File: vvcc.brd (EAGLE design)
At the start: 49 x 50 mm, 51 parts, among them IC1 MCP40D19T-5K, IC2 RP2040, IC3 NCP1117LPST33T3G, IC4 16MB_Flash, IC5 LD117ADT-TR, IC6 CLXC8T245QRHLRQ1, J1 Micro-B, J2 302-S301, J3 302-S301, Q1 12MHz

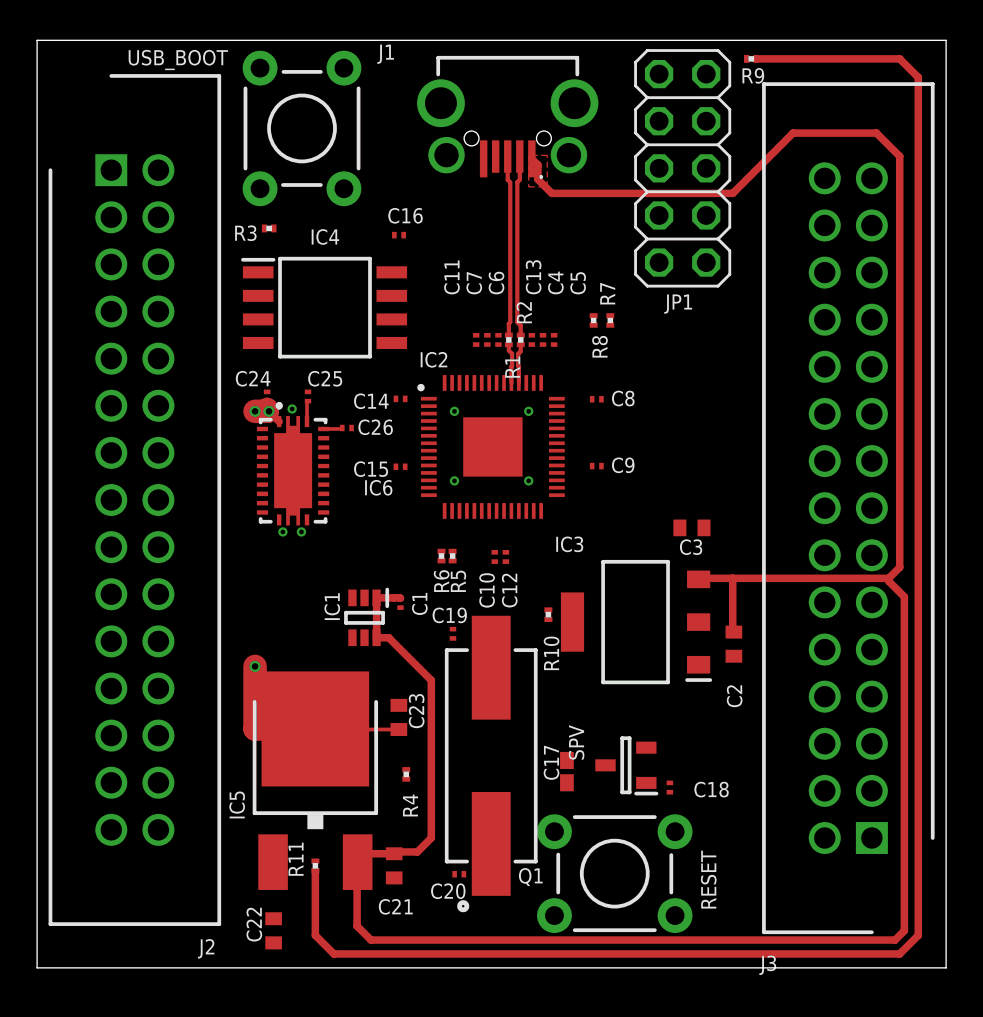
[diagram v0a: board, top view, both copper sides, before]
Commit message: Change the layout a little to group +5v closer together
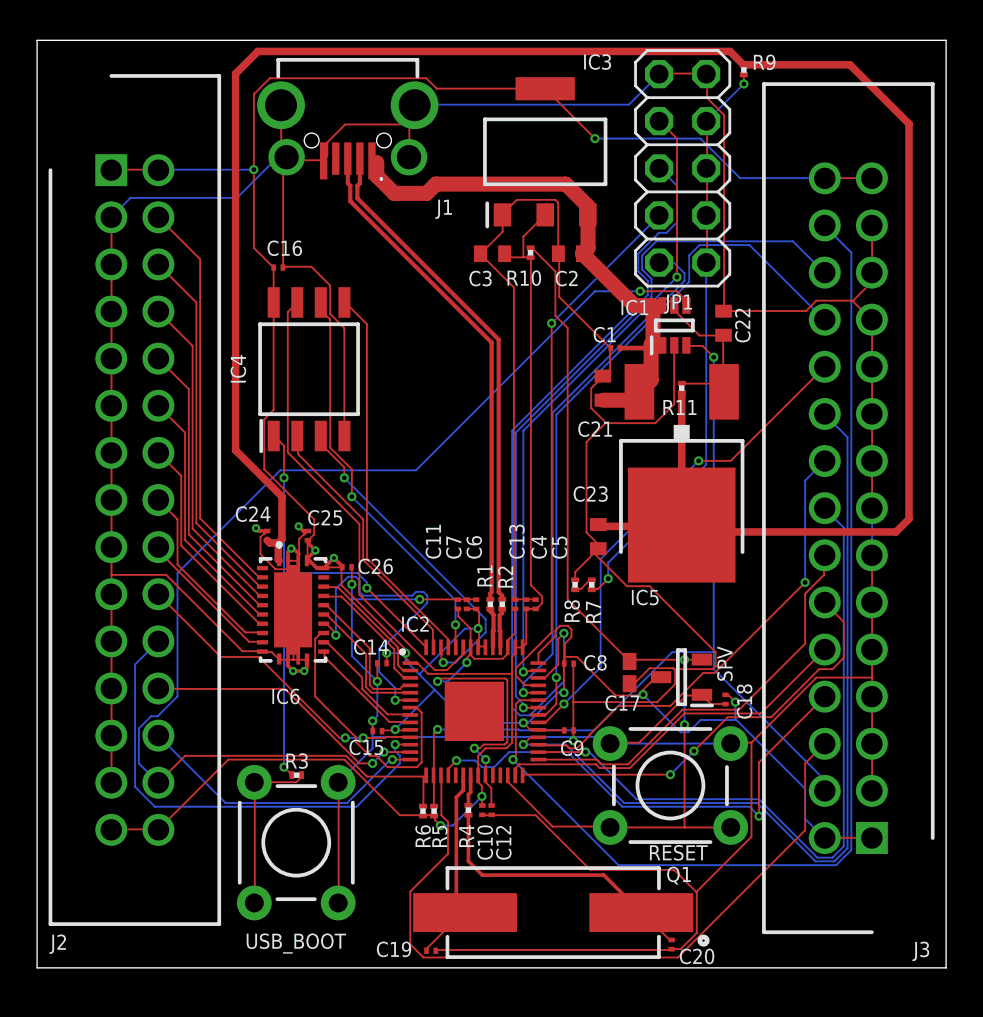
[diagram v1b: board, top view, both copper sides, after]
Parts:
- moved C22 40.8 mm to (37.0, 34.8), turned to 90 degrees
- moved USB_BOOT 38.5 mm to (14.0, 6.75), turned to 270 degrees
- moved R11 32.5 mm to (34.8, 31.2)
- moved R3 29.5 mm to (14.0, 10.4), turned to 180 degrees
- moved C21 28.1 mm to (30.5, 31.2), turned to 90 degrees
- moved IC3 25.8 mm to (27.4, 44.0), turned to 90 degrees
- moved IC5 25.3 mm to (34.8, 26.2), turned to 180 degrees
- moved IC1 23.0 mm to (34.4, 34.6), turned to 90 degrees
- moved C2 22.8 mm to (28.8, 38.5), turned to 180 degrees
- moved R10 19.5 mm to (26.6, 38.5)
- moved C3 18.3 mm to (24.6, 38.5)
- moved C1 18.0 mm to (31.2, 33.4), turned to 180 degrees
- moved C19 17.1 mm to (21.2, 0.92), turned to 0 degrees
- moved C23 14.5 mm to (30.2, 23.2), turned to 270 degrees
- moved C8 14.3 mm to (28.7, 16.4)
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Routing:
- net GND: track 0.00 -> 357.2 mm, vias 7 -> 10
- net +3V3: track 2.20 -> 208.0 mm, vias 0 -> 14
- net +5V: track 133.1 -> 31.6 mm
- net GPIO12: track 0.00 -> 64.2 mm, vias 0 -> 1
- net GPIO25: track 0.00 -> 59.5 mm, vias 0 -> 1
- net !RESET!: track 0.00 -> 51.1 mm, vias 0 -> 2
- net GPIO13: track 0.00 -> 48.5 mm, vias 0 -> 2
- net GPIO21: track 0.00 -> 45.3 mm, vias 0 -> 1
- net ADC2: track 0.00 -> 43.3 mm, vias 0 -> 1
- net GPIO14: track 0.00 -> 39.6 mm
- net GPIO24: track 0.00 -> 39.5 mm, vias 0 -> 1
- net GPIO19: track 0.00 -> 37.7 mm, vias 0 -> 1
- net GPIO23: track 0.00 -> 37.6 mm, vias 0 -> 1
- net ADC3: track 0.00 -> 34.4 mm, vias 0 -> 2
- net N$9: track 0.00 -> 31.5 mm, vias 0 -> 2
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- removed copper zone on layer 1, net +5V

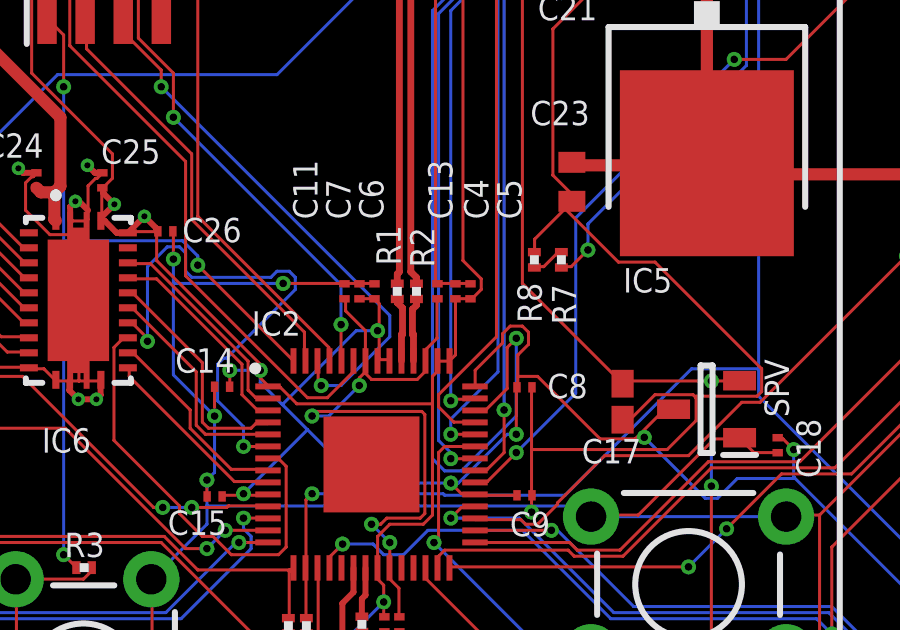
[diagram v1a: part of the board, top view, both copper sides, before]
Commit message: Add in a missing 0.1uF capacitor on +3v3
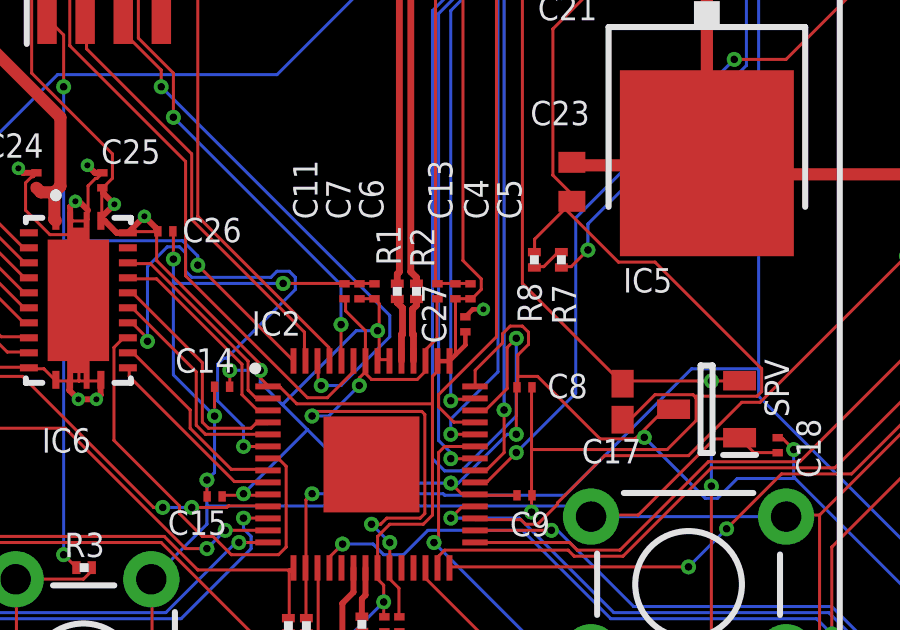
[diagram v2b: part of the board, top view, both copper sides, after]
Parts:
- added C27: 1uF, rcl:C0201
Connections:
- net +3V3: now also C27.1
- net GND: now also C27.2
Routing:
- net +3V3: track 208.0 -> 209.2 mm
- net GND: track 357.2 -> 358.0 mm, vias 10 -> 11
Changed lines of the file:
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@@
 <attribute name="VALUE" x="16.065" y="19.695" locked="yes" size="1.27" layer="27"/>
+</element>
+<element name="C27" library="rcl" library_urn="urn:adsk.eagle:library:334" package="C0201" package3d_urn="urn:adsk.eagle:package:23690/2" value="1uF" x="26.7" y="18.5" smashed="yes" rot="R90">
+<attribute name="NAME" x="26.065" y="17.865" size="0.8128" layer="25" rot="R90"/>
+<attribute name="POPULARITY" value="0" x="26.7" y="18.5" size="1.778" layer="27" rot="R90" display="off"/>
+<attribute name="SPICEPREFIX" value="C" x="26.7" y="18.5" size="1.778" layer="27" rot="R90" display="off"/>
+<attribute name="USE" value="0201B102K250CT" x="26.7" y="18.5" size="1.778" layer="27" rot="R90" display="off"/>
+<attribute name="VALUE" x="28.605" y="17.865" size="1.27" layer="27" rot="R90"/>
 </element>
 </elements>
@@
 <wire x1="14.540525" y1="16.640525" x2="14.55" y2="16.65" width="0.2" layer="1"/>
 <wire x1="14.540525" y1="16.140525" x2="14.540525" y2="16.640525" width="0.2" layer="1"/>
+<contactref element="C27" pad="2"/>
+<via x="27.3" y="19" extent="1-16" drill="0.2"/>
+<wire x1="26.7" y1="18.75" x2="26.95" y2="19" width="0.1524" layer="1"/>
+<wire x1="26.95" y1="19" x2="27.3" y2="19" width="0.1524" layer="1"/>
 </signal>
 <signal name="+3V3">
@@
 <wire x1="26.4144" y1="19.3548" x2="26.37" y2="19.35" width="0.1016" layer="1"/>
 <wire x1="26.8224" y1="19.3548" x2="26.87" y2="19.35" width="0.1016" layer="1"/>
-<wire x1="26.37" y1="17.48" x2="26.37" y2="19.35" width="0.1016" layer="1"/>
+<wire x1="26.37" y1="19.35" x2="26.37" y2="17.48" width="0.1016" layer="1"/>
 <wire x1="26.17" y1="17.28" x2="26.37" y2="17.48" width="0.1016" layer="1"/>
-<wire x1="26.162" y1="17.272" x2="25.8064" y2="17.272" width="0.1016" layer="1"/>
 <wire x1="25.8064" y1="17.272" x2="25.77" y2="17.28" width="0.1016" layer="1"/>
 <wire x1="26.162" y1="17.272" x2="26.17" y2="17.28" width="0.1016" layer="1"/>
@@
 <wire x1="15.45" y1="21.55" x2="15.0768" y2="21.55" width="0.2" layer="1"/>
 <wire x1="15.0768" y1="21.55" x2="15.0134" y2="21.6134" width="0.2" layer="1"/>
+<contactref element="C27" pad="1"/>
+<wire x1="26.7" y1="18.25" x2="26.7" y2="17.81" width="0.1524" layer="1"/>
+<wire x1="26.7" y1="17.81" x2="26.37" y2="17.48" width="0.1524" layer="1"/>
+<wire x1="26.37" y1="17.48" x2="26.162" y2="17.272" width="0.1524" layer="1"/>
+<wire x1="26.162" y1="17.272" x2="25.8064" y2="17.272" width="0.1524" layer="1"/>
 </signal>
 <signal name="+1.8_FT">

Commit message: Fix a few errors in the schematic. It is good to connect GND to the chip...
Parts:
- moved C16 9.66 mm to (21.5, 33.1)
- moved IC4 4.07 mm to (17.8, 29.6), turned to 0 degrees
- moved C17 0.75 mm to (31.9, 16.7)
- moved SPV 0.75 mm to (34.7, 16.4)
- moved C18 0.75 mm to (37.1, 15.2)
- moved RESET 0.56 mm to (33.9, 10.3)
- moved USB_BOOT 0.50 mm to (14.0, 6.25)
- moved R3 0.44 mm to (14.2, 10.8)
- moved C25 0.32 mm to (14.3, 23.2), turned to 180 degrees
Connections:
- new net SWCLK: IC2.24, J3.5
- new net SWDIO: IC2.25, J3.7
- net !RESET!: now also J3.3
- net GND: now also IC2.19, IC2.57; no longer J3.3, J3.5, J3.7
- net GPIO8: now also IC6.2
- net GPIO9: now also IC6.22
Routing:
- net GND: track 358.0 -> 112.0 mm, vias 11 -> 21
- net +3V3: track 209.2 -> 47.5 mm, vias 14 -> 16
- net SWDIO: track 0.00 -> 25.8 mm
- net SWCLK: track 0.00 -> 22.4 mm, vias 0 -> 1
- net GPIO8: track 16.8 -> 35.0 mm
- net GPIO21: track 45.3 -> 29.2 mm
- net GPIO25: track 59.5 -> 75.4 mm
- net GPIO14: track 39.6 -> 24.9 mm, vias 0 -> 2
- net !RESET!: track 51.1 -> 63.8 mm, vias 2 -> 0
- net GPIO15: track 27.1 -> 39.8 mm, vias 2 -> 1
- net GPIO22: track 26.8 -> 37.9 mm, vias 2 -> 1
- net LVL4: track 17.5 -> 6.81 mm, vias 2 -> 0
- net QSPI_SD3: track 25.6 -> 15.0 mm
- net QSPI_SD0: track 20.9 -> 10.8 mm
- net QSPI_CLK: track 21.6 -> 13.2 mm, vias 2 -> 0
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
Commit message: Submit for creation
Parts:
- C17: device rcl:C0402K -> rcl:C0402
- JP1: value (none) -> ADC_IO
- RESET: value RESET -> B3F-1005
- USB_BOOT: value USB_BOOT -> B3F-1005
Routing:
- net +3V3: track 47.5 -> 63.7 mm, vias 16 -> 26

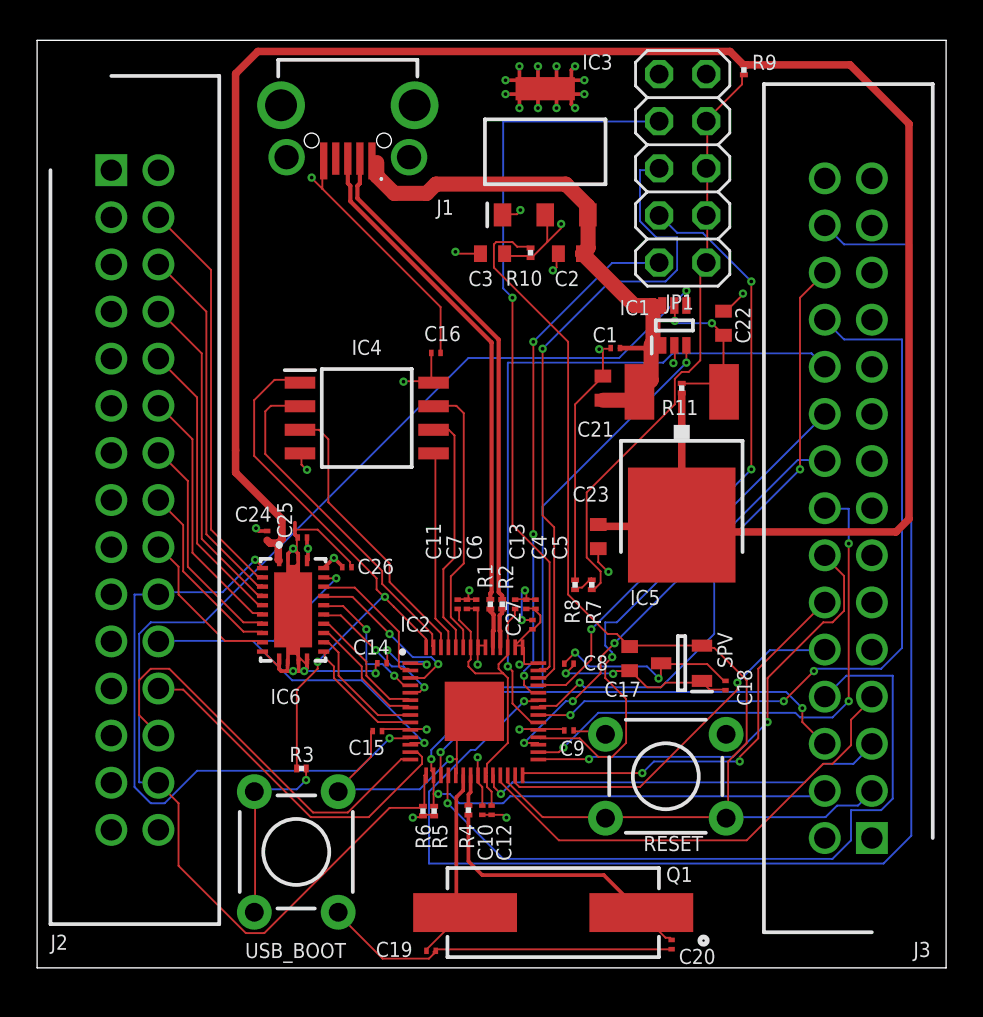
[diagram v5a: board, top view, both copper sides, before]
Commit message: Better board layout - and added LEDs. This was the real submit to nextpcb
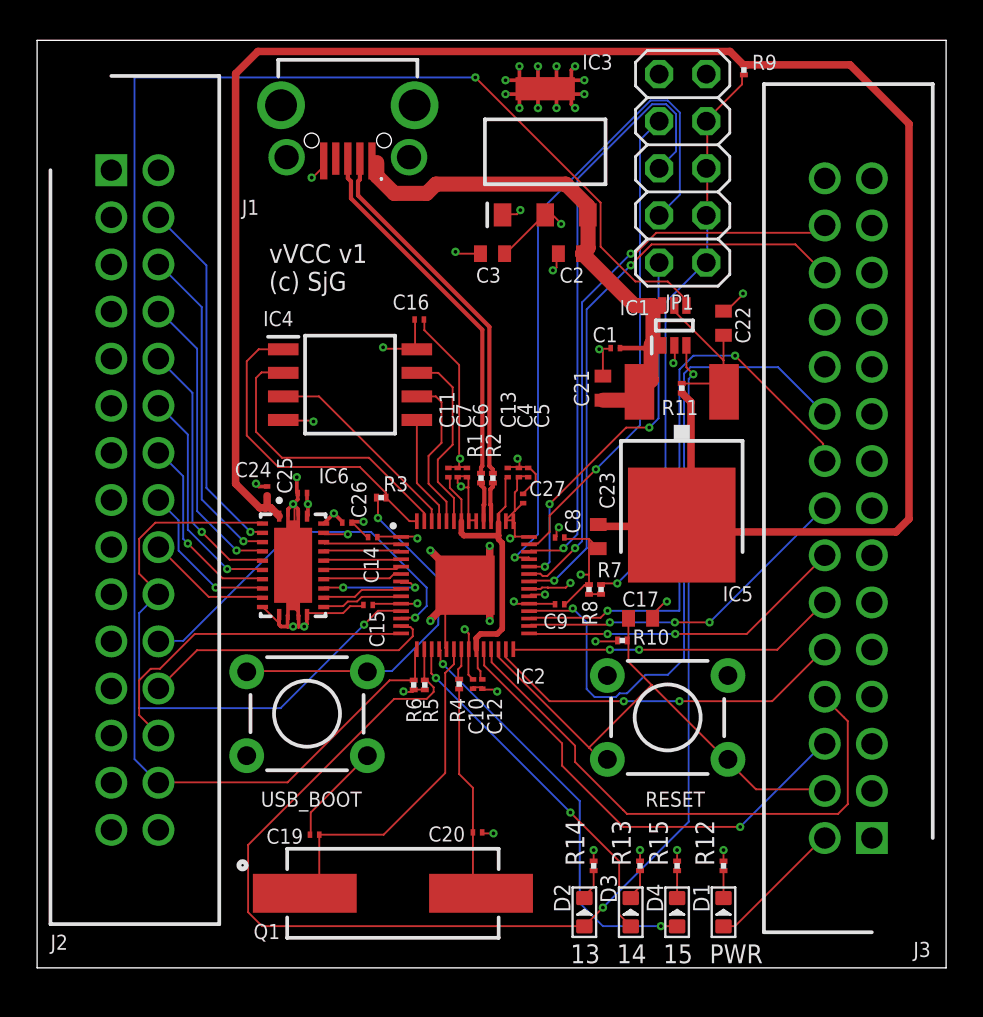
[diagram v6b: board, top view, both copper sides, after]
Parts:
- removed C18: 100nF, rcl:C0201
- removed SPV: MIC803-30D3VM3-TR, x-pi:SOT95P237X111-3N
- added D1, D2, D3, D4: GREEN, Seeed-LED:LED-0603
- added R12, R13, R14, R15: 1K, rcl:R0201
- moved R10 21.5 mm to (31.6, 17.6), turned to 180 degrees
- moved R3 15.2 mm to (18.6, 25.4), turned to 0 degrees
- moved C20 12.1 mm to (23.7, 7.30), turned to 180 degrees
- moved C19 8.87 mm to (15.0, 7.18), turned to 180 degrees
- moved Q1 8.70 mm to (19.2, 4.02), turned to 0 degrees
- moved USB_BOOT 7.47 mm to (14.6, 13.7), turned to 180 degrees
- moved C11 7.12 mm to (22.2, 26.7)
- moved C6 7.12 mm to (23.2, 26.7)
- moved C7 7.12 mm to (22.7, 26.7)
- moved C4 7.11 mm to (26.0, 26.7)
- moved C5 7.11 mm to (26.5, 26.7)
- moved C13 7.11 mm to (25.4, 26.7)
- moved C10 6.82 mm to (23.5, 15.3)
- moved C12 6.82 mm to (24.0, 15.3)
- moved C14 6.82 mm to (18.1, 23.2)
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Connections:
- new net N$1: C19.1, IC2.20, Q1.1
- new net N$2: C20.2, Q1.2, R4.1
- new net N$3: D1.-, R12.1
- new net N$4: D2.-, R14.1
- net !RESET!: now also J3.4; no longer J3.3, SPV.2
- net +3V3: now also D1.+; no longer C18.1, SPV.3
- net GND: now also J3.3, J3.5, J3.7, R12.2, R13.2, R14.2, R15.2; no longer C18.2, SPV.1
- net GPIO13: now also D2.+; no longer J3.4
- net GPIO14: now also D3.+; no longer J3.6
- net GPIO15: now also D4.+; no longer J3.8
- net N$6: now also D3.-, R13.1; no longer C19.1, IC2.20, Q1.2
- net N$8: now also D4.-, R15.1; no longer C20.2, Q1.1, R4.1
- net SWCLK: now also J3.6; no longer J3.5
- net SWDIO: now also J3.8; no longer J3.7
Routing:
- net GPIO25: track 75.4 -> 31.4 mm, vias 1 -> 2
- net GND: track 112.0 -> 76.0 mm, vias 21 -> 28
- net !RESET!: track 63.7 -> 29.3 mm
- net GPIO12: track 71.3 -> 92.8 mm
- net GPIO23: track 42.3 -> 22.2 mm, vias 3 -> 1
- net N$1: track 0.00 -> 18.5 mm
- net GPIO13: track 53.7 -> 71.9 mm, vias 3 -> 2
- net GPIO15: track 39.8 -> 22.6 mm, vias 1 -> 2
- net GPIO22: track 37.9 -> 21.9 mm
- net !QSPI_SS!: track 31.5 -> 17.5 mm, vias 2 -> 0
- net N$8: track 15.2 -> 1.48 mm
- net ADC3: track 39.5 -> 26.0 mm
- net N$2: track 0.00 -> 11.5 mm
- net GPIO19: track 29.8 -> 18.6 mm
- net N$5: track 10.3 -> 19.6 mm
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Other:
- board text added: "(c) SjG"
- board text added: "13"
- board text added: "14"
- board text added: "15"
- board text added: "PWR"
- board text added: "vVCC v1"
